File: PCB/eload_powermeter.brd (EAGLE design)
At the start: 100 x 100 mm, 78 parts, among them IC1 ADS1115_IC, IC2 SGM8582, IC3 TP4056, IC4 FS312F-G, IC5 MT3608, IC6 FS8205, K2 TXD2SA-4.5V, Q1 BSS123, Q3 BSS123, Q4 IRF520, Q5 BSS123, Q6 IRF520, Q7 IRF520, U1 ATMEGA328P, Y1 16MHz

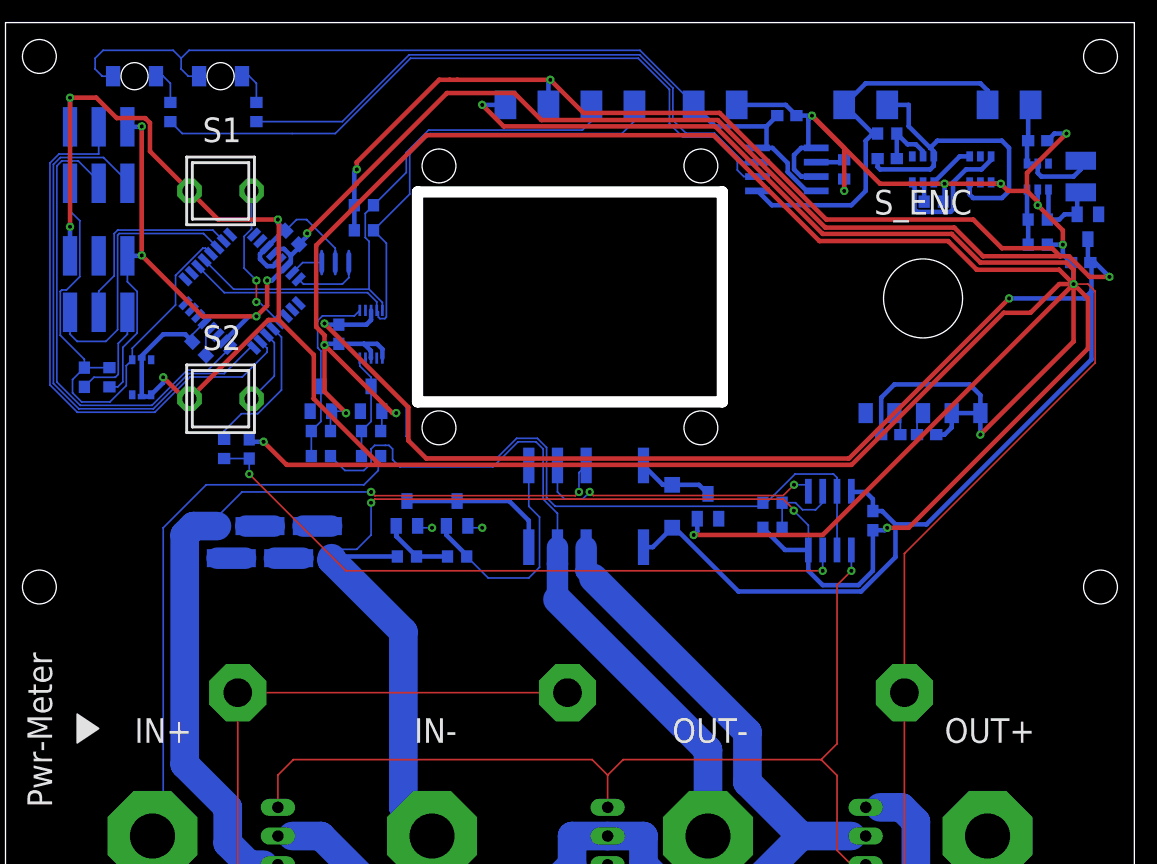
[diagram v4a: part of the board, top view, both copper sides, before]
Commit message: Adding some missing uC connections.
Adding some connections of the uC that were missing before.
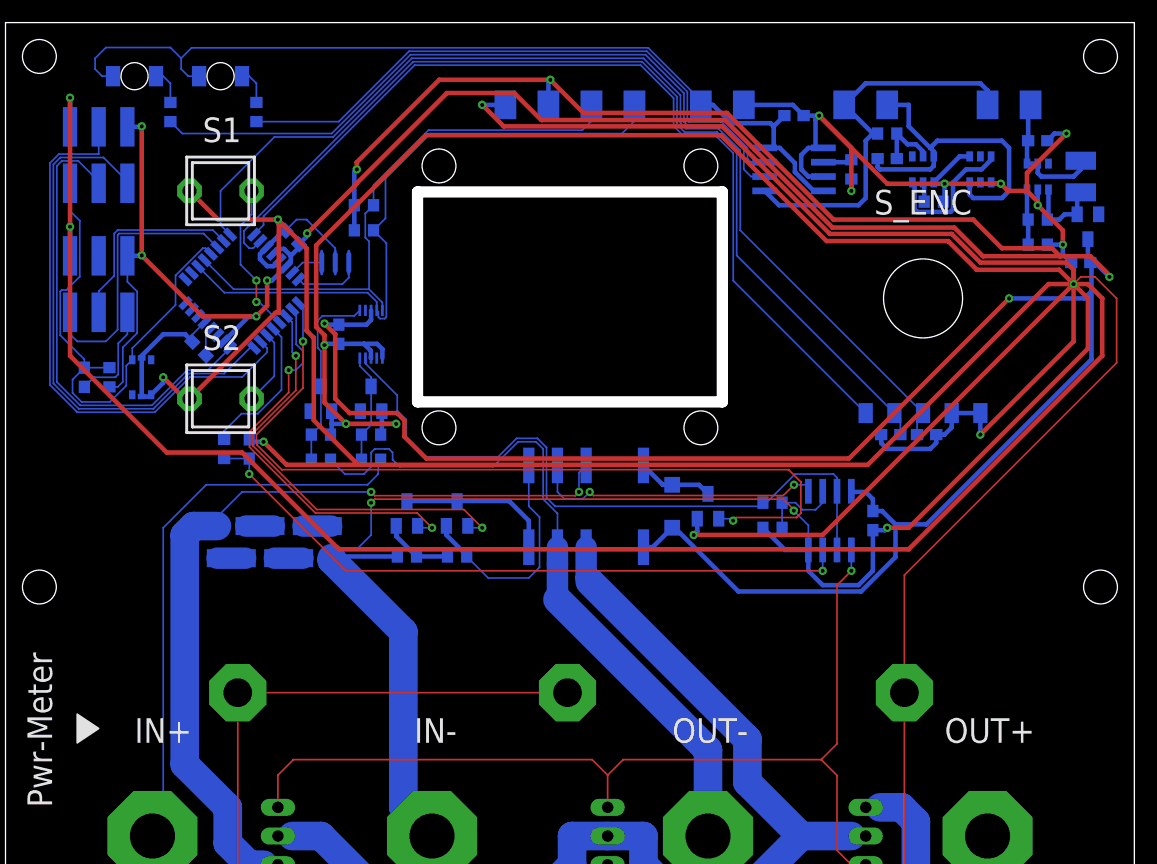
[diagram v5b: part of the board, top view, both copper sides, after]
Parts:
- moved R9 0.64 mm to (74.9, 87.0)
- moved VUSB- 0.64 mm to (65.4, 92.7)
- moved VUSB+ 0.63 mm to (61.6, 92.7)
- moved C9 0.63 mm to (69.8, 91.8)
- moved IC3 0.63 mm to (69.8, 87.0)
- moved R17 0.32 mm to (32.4, 63.5)
- moved R3 0.32 mm to (27.9, 63.5)
- moved R16 0.32 mm to (32.4, 61.3)
- moved R2 0.32 mm to (27.9, 61.3)
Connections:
- removed net SENSE_A3: IC1.7
- net ENC_A: now also U1.32
- net ENC_B: now also U1.2
- net MA: now also U1.10
- net RELAIS: now also U1.9
- net S_ENC: now also U1.1
- net UA: now also U1.11
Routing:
- net GND: track 838.4 -> 947.4 mm
- net ENC_A: track 2.13 -> 92.1 mm
- net ENC_B: track 2.13 -> 88.6 mm
- net S_ENC: track 0.00 -> 81.7 mm
- net RELAIS: track 0.00 -> 74.4 mm, vias 0 -> 2
- net UA: track 1.34 -> 38.1 mm, vias 1 -> 2
- net MA: track 1.34 -> 35.4 mm, vias 1 -> 2
- net +5V: track 376.0 -> 378.6 mm
- net N$27: track 52.4 -> 53.7 mm
- net VUSB: track 79.3 -> 80.6 mm
- net N$28: track 61.8 -> 63.0 mm

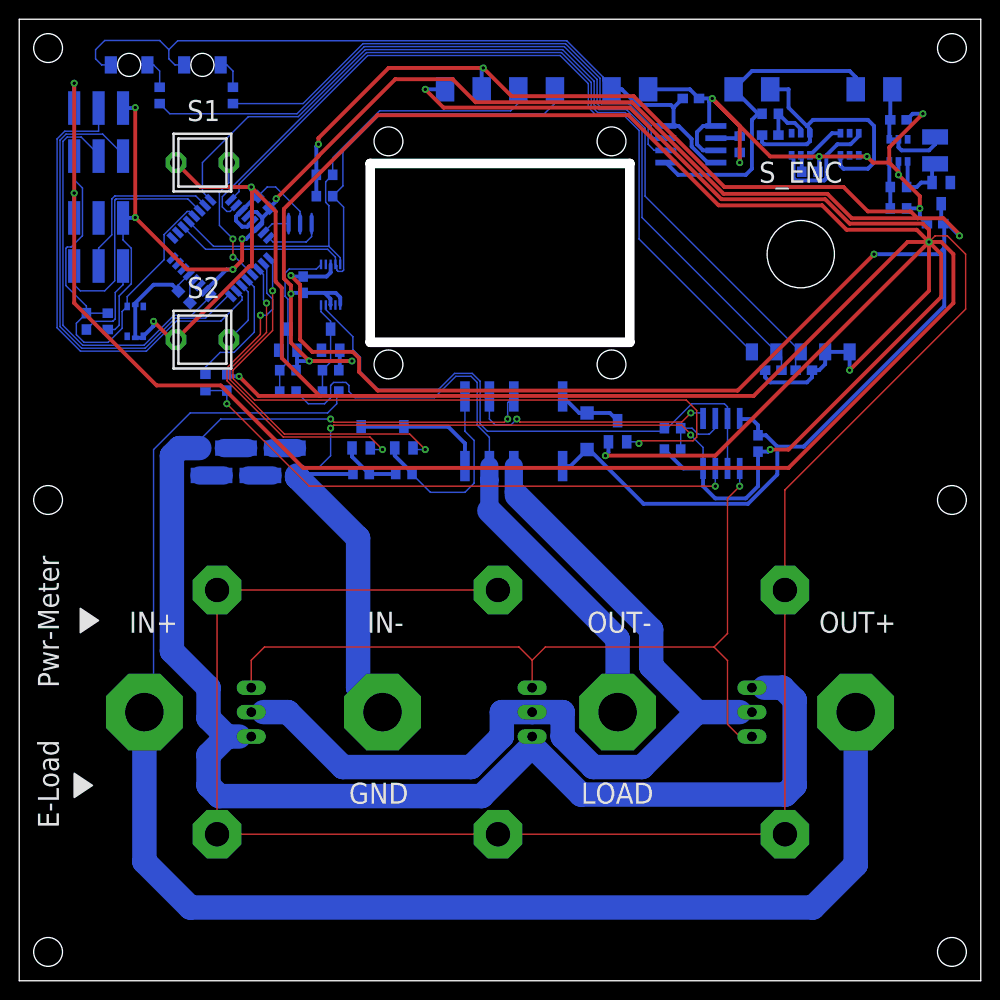
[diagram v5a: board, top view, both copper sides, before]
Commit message: Adding Battery measurement and power on led. Cleaning up silk screen.
Connecting both terminals of the battery  to adc pins of the uC to measure the battery capacity. Adding the connections of the power-on led that is build in to the button.
Cleaning up the component names of the silk screen.
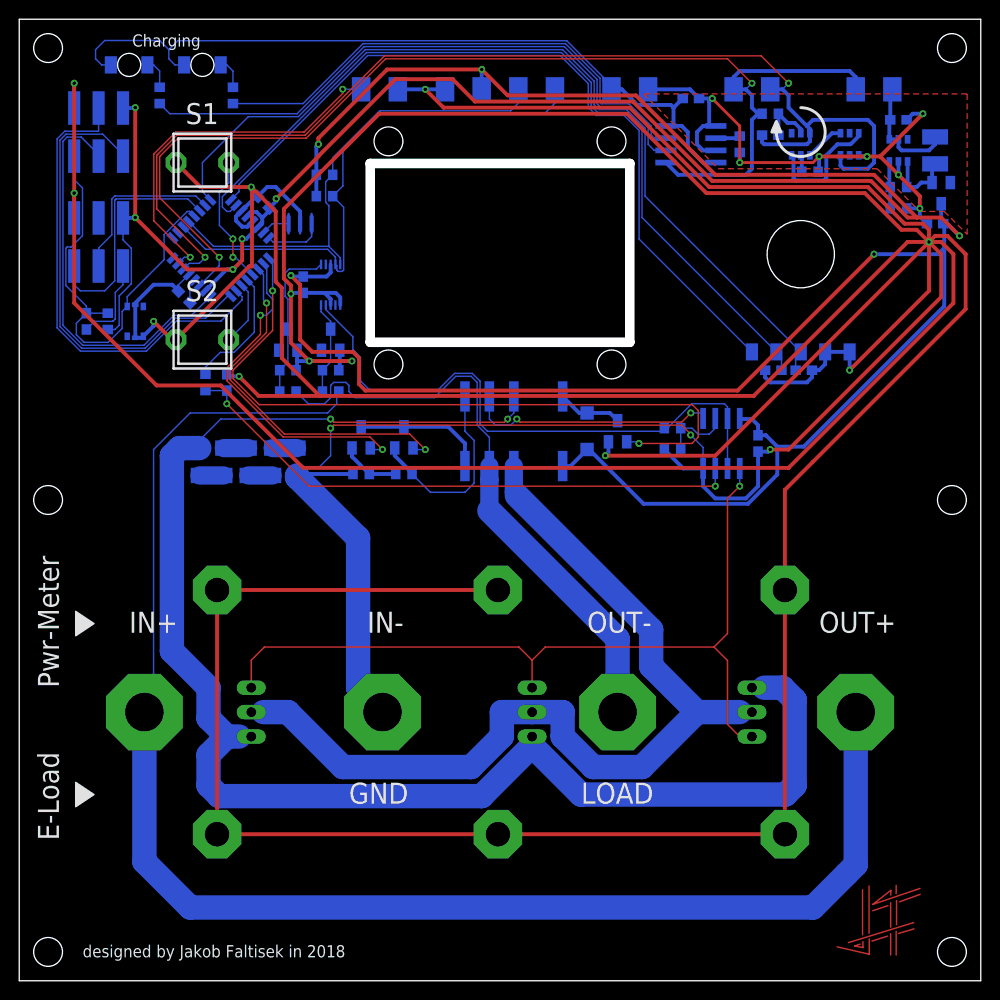
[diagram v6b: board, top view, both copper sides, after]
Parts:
- added LED_ON1, LED_ON2: SOLDER_PAD, eload_powermeter:SOLDER_PAD
- renumbered JP1 to ISP, JP2 to SERIAL, R9 to RPROG
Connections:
- new net LED_ON: LED_ON1.P$1, U1.23
- net GND: now also LED_ON2.P$1
- net VBAT+: now also U1.19
- net VBAT-: now also U1.22
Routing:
- net VBAT-: track 30.4 -> 118.5 mm, vias 0 -> 2
- net VBAT+: track 34.8 -> 120.8 mm, vias 0 -> 2
- net LED_ON: track 0.00 -> 38.5 mm, vias 0 -> 2
- net N$38: track 0.00 -> 8.08 mm
- net N$32: track 0.00 -> 7.10 mm
- net N$45: track 0.00 -> 5.03 mm
- net N$46: track 0.00 -> 4.92 mm
- net N$4: track 0.00 -> 4.68 mm
- net GND: track 947.4 -> 944.5 mm
- net N$36: track 0.00 -> 2.54 mm
- net N$35: track 0.00 -> 2.50 mm
- net N$42: track 0.00 -> 2.48 mm
- net N$37: track 0.00 -> 2.28 mm
- net N$43: track 0.00 -> 2.22 mm
- net N$26: track 0.00 -> 2.11 mm
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- added copper zone on layer 1, net GND
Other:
- board text added: "+"
- board text added: "-"
- board text added: "A"
- board text added: "B"
- board text added: "C"
- board text added: "Charging"
- board text added: "DTR"
- board text added: "LED_ON"
- board text added: "MISO"
- board text added: "MOSI"
- board text added: "RESET"
- board text added: "RST"
- board text added: "RX"
- board text added: "SCK"
- board text added: "SCL"
- board text added: "SDA"
- board text added: "SW+"
- board text added: "SW-"
- board text added: "SW_PWR"
- board text added: "TX"
- board text added: "VCC"
- board text added: "V_BAT"
- board text added: "V_USB"
- board text added: "designed by Jakob Faltisek in 2018"

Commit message: Final V1.0 Production Version
Finalising the V1.0 Production Version.
Generationg the gerbers and the BOM
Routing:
- net VBAT-: track 118.5 -> 117.6 mm
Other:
- board text added: "V1.0 - 0818"
- board text added: "designed by Jakob Faltisek"
- board text removed: "designed by Jakob Faltisek in 2018"
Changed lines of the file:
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@@
 <setting verticaltext="up"/>
 </settings>
-<grid distance="25" unitdist="mil" unit="mm" style="lines" multiple="1" display="yes" altdistance="6.25" altunitdist="mil" altunit="mm"/>
+<grid distance="25" unitdist="mil" unit="mm" style="dots" multiple="1" display="no" altdistance="6.25" altunitdist="mil" altunit="mm"/>
 <layers>
 <layer number="1" name="Top" color="4" fill="1" visible="yes" active="yes"/>
@@
 </layers>
 <board>
-<fusionsync huburn="a.cGVyc29uYWw6dWUyYWE1NDFk" projecturn="a.cGVyc29uYWw6dWUyYWE1NDFkIzIwMTcxMjA3MTA3NjA4MDU2" f3durn="urn:adsk.wipprod:dm.lineage:YlcdiyFwTF2Xg0Tt0ADviA" pcbguid="e0c28711-6ae4-45f4-8a2e-77067c162c65" lastpulledtime="" lastsyncedchangeguid="0ea3246f-613a-8673-2bc7-e3b06efad715"/>
+<fusionsync huburn="a.cGVyc29uYWw6dWUyYWE1NDFk" projecturn="a.cGVyc29uYWw6dWUyYWE1NDFkIzIwMTcxMjA3MTA3NjA4MDU2" f3durn="urn:adsk.wipprod:dm.lineage:YlcdiyFwTF2Xg0Tt0ADviA" pcbguid="e0c28711-6ae4-45f4-8a2e-77067c162c65" lastpulledtime="" lastsyncedchangeguid="7b7d046e-6902-2b37-0383-acbd50ea6bdf"/>
 <plain>
 <wire x1="0" y1="0" x2="100" y2="0" width="0" layer="20"/>
@@
 <vertex x="7.77875" y="37.1475"/>
 </polygon>
-<text x="11.7475" y="97.155" size="1.27" layer="21">Charging</text>
+<text x="11.7475" y="97.79" size="1.27" layer="21">Charging</text>
 <text x="40.3225" y="95.885" size="1.016" layer="22" rot="MR0">LED_ON</text>
 <text x="36.03625" y="94.2975" size="1.016" layer="22" rot="MR0">+</text>
 <text x="39.6875" y="94.45625" size="1.016" layer="22" rot="MR0">-</text>
-<text x="45.56125" y="90.01125" size="0.8128" layer="22" rot="MR0">GND</text>
-<text x="49.2125" y="90.01125" size="0.8128" layer="22" rot="MR0">VCC</text>
-<text x="52.86375" y="90.01125" size="0.8128" layer="22" rot="MR0">SCL</text>
-<text x="56.99125" y="90.01125" size="0.8128" layer="22" rot="MR0">SDA</text>
+<text x="45.24375" y="94.45625" size="0.8128" layer="22" rot="MR0">GND</text>
+<text x="48.895" y="94.45625" size="0.8128" layer="22" rot="MR0">VCC</text>
+<text x="52.705" y="94.45625" size="0.8128" layer="22" rot="MR0">SCL</text>
+<text x="56.8325" y="94.45625" size="0.8128" layer="22" rot="MR0">SDA</text>
 <text x="65.7225" y="95.885" size="1.016" layer="22" rot="MR0">V_USB</text>
 <text x="61.9125" y="94.45625" size="1.016" layer="22" rot="MR0">+</text>
@@
 <wire x1="88.9" y1="94.615" x2="88.9" y2="95.09125" width="0.1524" layer="22"/>
 <wire x1="89.2175" y1="95.09125" x2="88.5825" y2="95.09125" width="0.1524" layer="22"/>
-<text x="6.82625" y="83.97875" size="1.016" layer="22" rot="MR180">SCK</text>
-<text x="3.4925" y="83.97875" size="1.016" layer="22" rot="MR180">RST</text>
-<text x="10.16" y="83.97875" size="1.016" layer="22" rot="MR180">MISO</text>
-<text x="6.19125" y="93.50375" size="1.016" layer="22" rot="MR180">MOSI</text>
-<text x="5.23875" y="92.55125" size="1.016" layer="22" rot="MR0">GND</text>
-<text x="10.31875" y="93.50375" size="1.016" layer="22" rot="MR180">VCC</text>
+<text x="6.82625" y="83.82" size="1.016" layer="22" rot="MR180">SCK</text>
+<text x="3.4925" y="83.82" size="1.016" layer="22" rot="MR180">RST</text>
+<text x="10.16" y="83.82" size="1.016" layer="22" rot="MR180">MISO</text>
+<text x="6.50875" y="93.6625" size="1.016" layer="22" rot="MR180">MOSI</text>
+<text x="5.08" y="92.71" size="1.016" layer="22" rot="MR0">GND</text>
+<text x="10.31875" y="93.6625" size="1.016" layer="22" rot="MR180">VCC</text>
 <text x="7.46125" y="72.39" size="1.016" layer="22" rot="MR180">TX</text>
 <text x="4.445" y="72.39" size="1.016" layer="22" rot="MR180">RX</text>
 <text x="10.16" y="72.39" size="1.016" layer="22" rot="MR180">DTR</text>
 <text x="10.00125" y="82.2325" size="1.016" layer="22" rot="MR180">VCC</text>
-<text x="5.3975" y="81.28" size="1.016" layer="22" rot="MR0">GND</text>
+<text x="5.08" y="81.28" size="1.016" layer="22" rot="MR0">GND</text>
 <text x="12.7" y="66.04" size="1.27" layer="22" rot="MR270">RESET</text>
 <text x="80.80375" y="66.675" size="1.016" layer="22" rot="MR90">A</text>
@@
 <rectangle x1="88.23325" y1="9.93013125" x2="88.39326875" y2="9.94790625" layer="200"/>
 <rectangle x1="91.113609375" y1="9.93013125" x2="91.273628125" y2="9.94790625" layer="200"/>
-<text x="6.59638125" y="2.435859375" size="1.27" layer="21" font="vector">designed by Jakob Faltisek in 2018</text>
+<text x="6.59638125" y="2.435859375" size="1.27" layer="21" font="vector">designed by Jakob Faltisek</text>
 <wire x1="87.709375" y1="9.46546875" x2="87.709375" y2="4.78234375" width="0.2" layer="29"/>
 <wire x1="87.7490625" y1="4.06796875" x2="87.7490625" y2="3.4528125" width="0.2" layer="29"/>
@@
 <wire x1="88.40390625" y1="2.75828125" x2="85.0503125" y2="3.5321875" width="0.2" layer="29"/>
 <wire x1="88.3840625" y1="4.94109375" x2="88.3840625" y2="9.86234375" width="0.2" layer="29"/>
+<text x="94.36861875" y="2.435859375" size="1.27" layer="22" font="vector" rot="MR0">V1.0 - 0818</text>
 </plain>
 <attributes>
@@
 <wire x1="9.2075" y1="67.73" x2="9.94686875" y2="67.73" width="0.1524" layer="16"/>
 <wire x1="96.2025" y1="76.2" x2="95.5675" y2="75.565" width="0.4064" layer="16"/>
-<via x="48.10125" y="94.77375" extent="1-16" drill="0.35"/>
-<wire x1="48.095" y1="92.71" x2="48.095" y2="94.7675" width="0.4064" layer="16"/>
-<wire x1="48.095" y1="94.7675" x2="48.10125" y2="94.77375" width="0.4064" layer="16"/>
-<wire x1="39.11076875" y1="93.7613" x2="45.07145" y2="93.7613" width="0.4064" layer="1"/>
+<wire x1="39.11076875" y1="93.7613" x2="44.9127" y2="93.7613" width="0.4064" layer="1"/>
 <wire x1="39.11076875" y1="93.7613" x2="31.115" y2="85.76553125" width="0.4064" layer="1"/>
 <wire x1="31.115" y1="85.725" x2="26.719528125" y2="81.329528125" width="0.4064" layer="1"/>
@@
 <wire x1="97.79" y1="77.47" x2="96.52" y2="78.74" width="0.4064" layer="16"/>
 <wire x1="96.52" y1="78.74" x2="96.1" y2="78.74" width="0.4064" layer="16"/>
-<wire x1="48.10125" y1="94.77375" x2="38.25875" y2="94.77375" width="0.4064" layer="1"/>
 <via x="31.115" y="86.995" extent="1-16" drill="0.35"/>
 <wire x1="30.9" y1="83.82" x2="30.9" y2="86.78" width="0.4064" layer="16"/>
 <wire x1="30.9" y1="86.78" x2="31.115" y2="86.995" width="0.4064" layer="16"/>
-<wire x1="31.115" y1="87.63" x2="38.25875" y2="94.77375" width="0.4064" layer="1"/>
+<wire x1="38.25875" y1="94.77375" x2="31.115" y2="87.63" width="0.4064" layer="1"/>
 <wire x1="31.115" y1="86.995" x2="31.115" y2="87.63" width="0.4064" layer="1"/>
 <wire x1="21.59" y1="73.9775" x2="22.225" y2="73.9775" width="0.4064" layer="16"/>
@@
 <wire x1="88.5825" y1="83.185" x2="72.0725" y2="83.185" width="0.4064" layer="1"/>
 <wire x1="72.0725" y1="83.185" x2="63.8175" y2="91.44" width="0.4064" layer="1"/>
-<wire x1="45.07145" y1="93.7613" x2="47.39275" y2="91.44" width="0.4064" layer="1"/>
-<wire x1="47.39275" y1="91.44" x2="63.8175" y2="91.44" width="0.4064" layer="1"/>
-<wire x1="48.10125" y1="94.77375" x2="50.8" y2="92.075" width="0.4064" layer="1"/>
+<wire x1="44.9127" y1="93.7613" x2="47.234" y2="91.44" width="0.4064" layer="1"/>
+<wire x1="47.234" y1="91.44" x2="63.8175" y2="91.44" width="0.4064" layer="1"/>
+<wire x1="49.68875" y1="92.71" x2="50.32375" y2="92.075" width="0.4064" layer="1"/>
 <wire x1="88.9" y1="83.82" x2="93.345" y2="79.375" width="0.4064" layer="1"/>
-<wire x1="50.8" y1="92.075" x2="64.135" y2="92.075" width="0.4064" layer="1"/>
+<wire x1="50.32375" y1="92.075" x2="64.135" y2="92.075" width="0.4064" layer="1"/>
 <wire x1="64.135" y1="92.075" x2="72.39" y2="83.82" width="0.4064" layer="1"/>
 <wire x1="72.39" y1="83.82" x2="88.9" y2="83.82" width="0.4064" layer="1"/>
+<wire x1="48.095" y1="92.71" x2="49.68875" y2="92.71" width="0.4064" layer="16"/>
+<via x="49.68875" y="92.71" extent="1-16" drill="0.35"/>
+<wire x1="49.68875" y1="92.71" x2="47.625" y2="94.77375" width="0.4064" layer="1"/>
+<wire x1="47.625" y1="94.77375" x2="38.25875" y2="94.77375" width="0.4064" layer="1"/>
 </signal>
 <signal name="N$8">
@@
 <wire x1="19.3238" y1="75.2475" x2="14.3002" y2="80.2711" width="0.1524" layer="1"/>
 <wire x1="14.3002" y1="80.2711" x2="14.3002" y2="85.85125625" width="0.1524" layer="1"/>
-<wire x1="78.74" y1="93.345" x2="78.105" y2="92.71" width="0.4064" layer="16"/>
 <wire x1="78.105" y1="92.71" x2="79.375" y2="92.71" width="0.4064" layer="16"/>
 <wire x1="79.375" y1="92.71" x2="80.01" y2="92.075" width="0.4064" layer="16"/>
@@
 <mfgpreviewcolor name="silkscreencolor" color="0xFFFEFEFE"/>
 <mfgpreviewcolor name="backgroundcolor" color="0xFF282828"/>
-<mfgpreviewcolor name="coppercolor" color="0xFFFFBF00"/>
+<mfgpreviewcolor name="coppercolor" color="0xFFCACACA"/>
 <mfgpreviewcolor name="substratecolor" color="0xFF786E46"/>
 </mfgpreviewcolors>
